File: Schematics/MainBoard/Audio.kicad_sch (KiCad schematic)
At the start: 13 parts, among them J6 AudioJack3, U11 LM386

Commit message: Work on PCB
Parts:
- added C69: 100uF 10V Tant, Capacitor_Tantalum_SMD:CP_EIA-7343-30_AVX-N, symbol Device:C_Polarized
- C46, C55: footprint Capacitor_SMD:C_0603_1608Metric -> Capacitor_SMD:C_0402_1005Metric
- C56: value 250uF 16V -> 100uF 10V Tant; footprint Capacitor_SMD:CP_Elec_10x12.5 -> Capacitor_Tantalum_SMD:CP_EIA-7343-30_AVX-N; LCSC DNF -> DNP; Mouser Part Number 667-EEV-FK1V681Q -> (none)
- LS1: footprint CMS160925078SP67 -> CMS-160925-078SP-67:CMS160925078SP67
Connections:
- net at C45.1, C55.1, C56.1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: now also C69.1
- net at C56.2, LS1.2 (+): now also C69.2
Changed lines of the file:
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@@
+	)
+	(junction
+		(at 229.87 92.71)
+		(diameter 0)
+		(color 0 0 0 0)
 	)
 	(junction
@@
 	)
 	(junction
+		(at 213.36 92.71)
+		(diameter 0)
+		(color 0 0 0 0)
+	)
+	(junction
 		(at 81.28 90.17)
 		(diameter 0)
@@
 	(wire
 		(pts
+			(xy 213.36 92.71) (xy 218.44 92.71)
+		)
+		(stroke
+			(width 0)
+			(type default)
+		)
+	)
+	(wire
+		(pts
 			(xy 156.21 107.95) (xy 163.83 107.95)
 		)
@@
 	(wire
 		(pts
+			(xy 226.06 80.01) (xy 229.87 80.01)
+		)
+		(stroke
+			(width 0)
+			(type default)
+		)
+	)
+	(wire
+		(pts
 			(xy 114.3 166.37) (xy 116.84 166.37)
 		)
@@
 	(wire
 		(pts
+			(xy 213.36 80.01) (xy 213.36 92.71)
+		)
+		(stroke
+			(width 0)
+			(type default)
+		)
+	)
+	(wire
+		(pts
 			(xy 128.27 80.01) (xy 134.62 80.01)
 		)
@@
 	(wire
 		(pts
-			(xy 187.96 92.71) (xy 218.44 92.71)
+			(xy 187.96 92.71) (xy 213.36 92.71)
 		)
 		(stroke
@@
 	(wire
 		(pts
+			(xy 218.44 80.01) (xy 213.36 80.01)
+		)
+		(stroke
+			(width 0)
+			(type default)
+		)
+	)
+	(wire
+		(pts
 			(xy 45.72 140.97) (xy 58.42 140.97)
 		)
@@
 	(wire
 		(pts
+			(xy 229.87 80.01) (xy 229.87 92.71)
+		)
+		(stroke
+			(width 0)
+			(type default)
+		)
+	)
+	(wire
+		(pts
 			(xy 81.28 90.17) (xy 129.54 90.17)
 		)
@@
 	(wire
 		(pts
-			(xy 226.06 92.71) (xy 237.49 92.71)
+			(xy 226.06 92.71) (xy 229.87 92.71)
 		)
 		(stroke
@@
 		(pts
 			(xy 187.96 111.76) (xy 187.96 114.3)
+		)
+		(stroke
+			(width 0)
+			(type default)
+		)
+	)
+	(wire
+		(pts
+			(xy 229.87 92.71) (xy 237.49 92.71)
 		)
 		(stroke
@@
 				(path "/a2243a34-697c-4939-97f7-df548e421864/598e71c9-5c06-425f-ac54-aba71004555d"
 					(reference "#PWR0185")
-					(unit 1)
-				)
-			)
-		)
-	)
-	(symbol
-		(lib_id "Device:C_Polarized")
-		(at 222.25 92.71 90)
-		(unit 1)
-		(exclude_from_sim no)
-		(in_bom yes)
-		(on_board yes)
-		(dnp no)
-		(fields_autoplaced yes)
-		(property "Reference" "C56"
-			(at 221.361 85.09 90)
-			(effects
-				(font
-					(size 1.27 1.27)
-				)
-			)
-		)
-		(property "Value" "250uF 16V"
-			(at 221.361 87.63 90)
-			(effects
-				(font
-					(size 1.27 1.27)
-				)
-			)
-		)
-		(property "Footprint" "Capacitor_SMD:CP_Elec_10x12.5"
-			(at 226.06 91.7448 0)
-			(effects
-				(font
-					(size 1.27 1.27)
-				)
-				(hide yes)
-			)
-		)
-		(property "Datasheet" "~"
-			(at 222.25 92.71 0)
-			(effects
-				(font
-					(size 1.27 1.27)
-				)
-				(hide yes)
-			)
-		)
-		(property "Description" "Polarized capacitor"
-			(at 222.25 92.71 0)
-			(effects
-				(font
-					(size 1.27 1.27)
-				)
-				(hide yes)
-			)
-		)
-		(property "Mouser Part Number" "667-EEV-FK1V681Q"
-			(at 222.25 92.71 90)
-			(effects
-				(font
-					(size 1.27 1.27)
-				)
-				(hide yes)
-			)
-		)
-		(property "LCSC" "DNF"
-			(at 222.25 92.71 90)
-			(effects
-				(font
-					(size 1.27 1.27)
-				)
-				(hide yes)
-			)
-		)
-		(pin "1"
-		)
-		(pin "2"
-		)
-		(instances
-			(project ""
-				(path "/a2243a34-697c-4939-97f7-df548e421864/598e71c9-5c06-425f-ac54-aba71004555d"
-					(reference "C56")
 					(unit 1)
 				)
@@
 	)
 	(symbol
+		(lib_id "Device:C_Polarized")
+		(at 222.25 80.01 90)
+		(unit 1)
+		(exclude_from_sim no)
+		(in_bom yes)
+		(on_board yes)
+		(dnp no)
+		(property "Reference" "C69"
+			(at 220.472 73.66 90)
+			(effects
+				(font
+					(size 1.27 1.27)
+				)
+			)
+		)
+		(property "Value" "100uF 10V Tant"
+			(at 226.314 75.692 90)
+			(effects
+				(font
+					(size 1.27 1.27)
+				)
+			)
+		)
+		(property "Footprint" "Capacitor_Tantalum_SMD:CP_EIA-7343-30_AVX-N"
+			(at 226.06 79.0448 0)
+			(effects
+				(font
+					(size 1.27 1.27)
+				)
+				(hide yes)
+			)
+		)
+		(property "Datasheet" "~"
+			(at 222.25 80.01 0)
+			(effects
+				(font
+					(size 1.27 1.27)
+				)
+				(hide yes)
+			)
+		)
+		(property "Description" "Polarized capacitor"
+			(at 222.25 80.01 0)
+			(effects
+				(font
+					(size 1.27 1.27)
+				)
+				(hide yes)
+			)
+		)
+		(property "LCSC" "DNP"
+			(at 222.25 80.01 0)
+			(effects
+				(font
+					(size 1.27 1.27)
+				)
+				(hide yes)
+			)
+		)
+		(pin "1"
+		)
+		(pin "2"
+		)
+		(instances
+			(project "MainBoard"
+				(path "/a2243a34-697c-4939-97f7-df548e421864/598e71c9-5c06-425f-ac54-aba71004555d"
+					(reference "C69")
+					(unit 1)
+				)
+			)
+		)
+	)
+	(symbol
 		(lib_id "power:GND")
 		(at 121.92 102.87 0)
@@
 			)
 		)
-		(property "Footprint" "CMS160925078SP67"
+		(property "Footprint" "CMS-160925-078SP-67:CMS160925078SP67"
 			(at 248.92 195.25 0)
 			(effects
@@
 			)
 		)
-		(property "Footprint" "Capacitor_SMD:C_0603_1608Metric"
+		(property "Footprint" "Capacitor_SMD:C_0402_1005Metric"
 			(at 128.27 79.0448 0)
 			(effects
@@
 				(path "/a2243a34-697c-4939-97f7-df548e421864/598e71c9-5c06-425f-ac54-aba71004555d"
 					(reference "C46")
+					(unit 1)
+				)
+			)
+		)
+	)
+	(symbol
+		(lib_id "Device:C_Polarized")
+		(at 222.25 92.71 90)
+		(unit 1)
+		(exclude_from_sim no)
+		(in_bom yes)
+		(on_board yes)
+		(dnp no)
+		(property "Reference" "C56"
+			(at 220.472 86.36 90)
+			(effects
+				(font
+					(size 1.27 1.27)
+				)
+			)
+		)
+		(property "Value" "100uF 10V Tant"
+			(at 226.314 88.392 90)
+			(effects
+				(font
+					(size 1.27 1.27)
+				)
+			)
+		)
+		(property "Footprint" "Capacitor_Tantalum_SMD:CP_EIA-7343-30_AVX-N"
+			(at 226.06 91.7448 0)
+			(effects
+				(font
+					(size 1.27 1.27)
+				)
+				(hide yes)
+			)
+		)
+		(property "Datasheet" "~"
+			(at 222.25 92.71 0)
+			(effects
+				(font
+					(size 1.27 1.27)
+				)
+				(hide yes)
+			)
+		)
+		(property "Description" "Polarized capacitor"
+			(at 222.25 92.71 0)
+			(effects
+				(font
+					(size 1.27 1.27)
+				)
+				(hide yes)
+			)
+		)
+		(property "LCSC" "DNP"
+			(at 222.25 92.71 0)
+			(effects
+				(font
+					(size 1.27 1.27)
+				)
+				(hide yes)
+			)
+		)
+		(pin "1"
+		)
+		(pin "2"
+		)
+		(instances
+			(project "MainBoard"
+				(path "/a2243a34-697c-4939-97f7-df548e421864/598e71c9-5c06-425f-ac54-aba71004555d"
+					(reference "C56")
 					(unit 1)
 				)
@@
 			)
 		)
-		(property "Footprint" "Capacitor_SMD:C_0603_1608Metric"
+		(property "Footprint" "Capacitor_SMD:C_0402_1005Metric"
 			(at 188.9252 101.6 0)
 			(effects

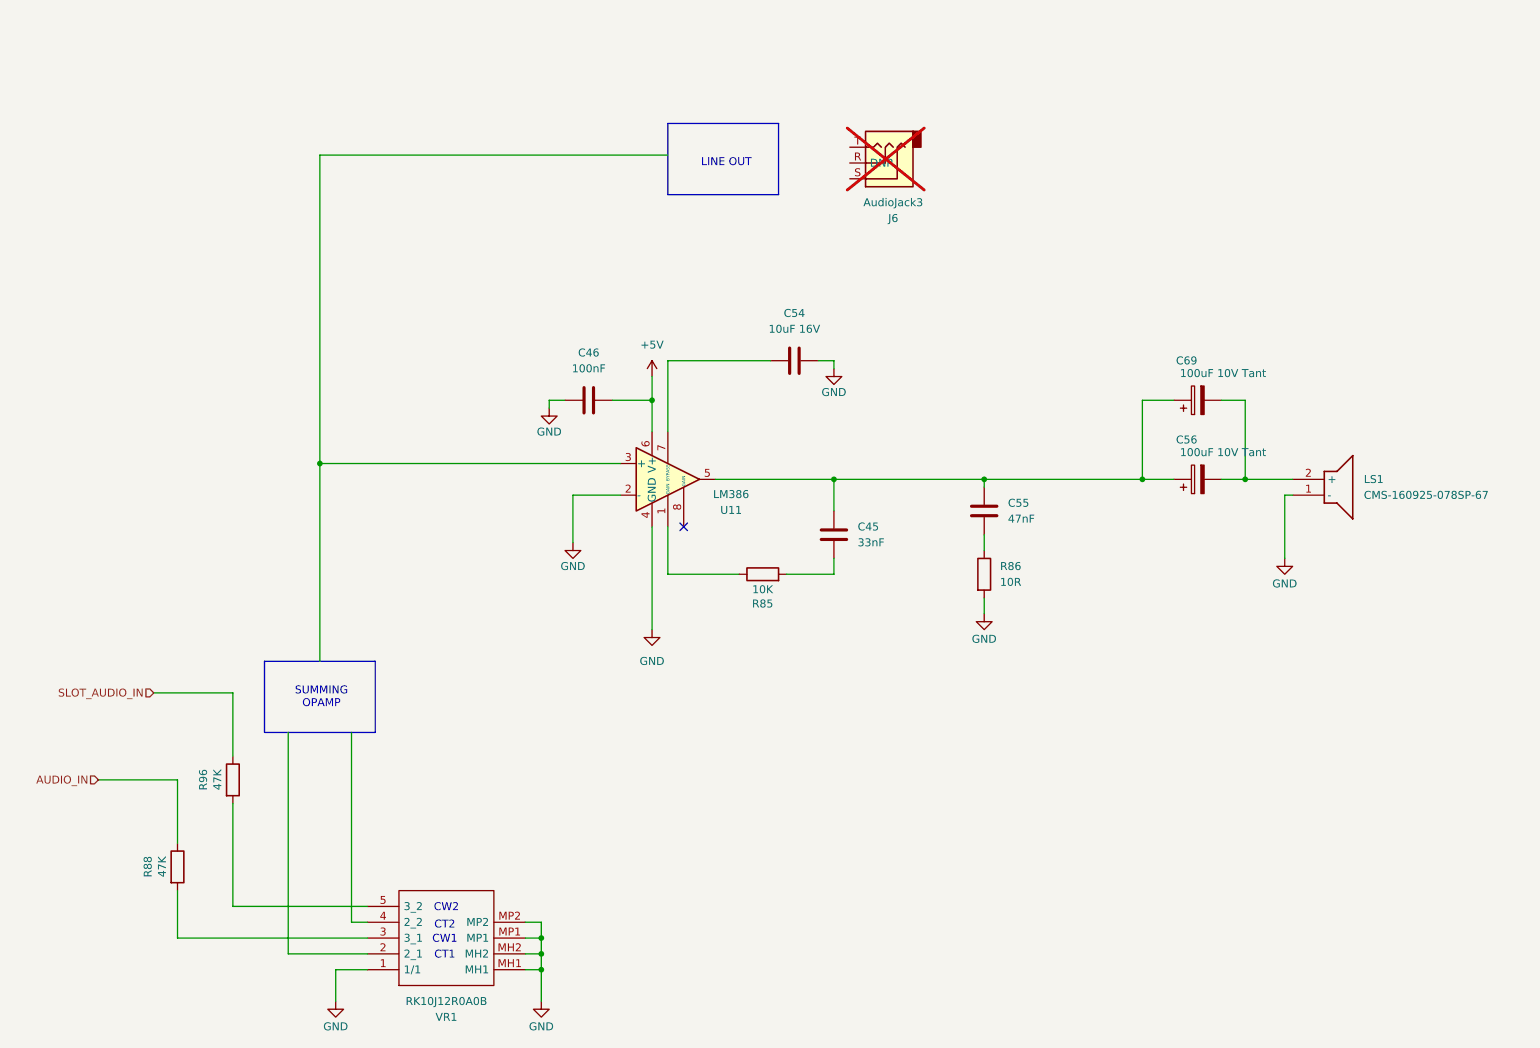
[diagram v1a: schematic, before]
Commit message: Work on PCB routing, added SwinSID
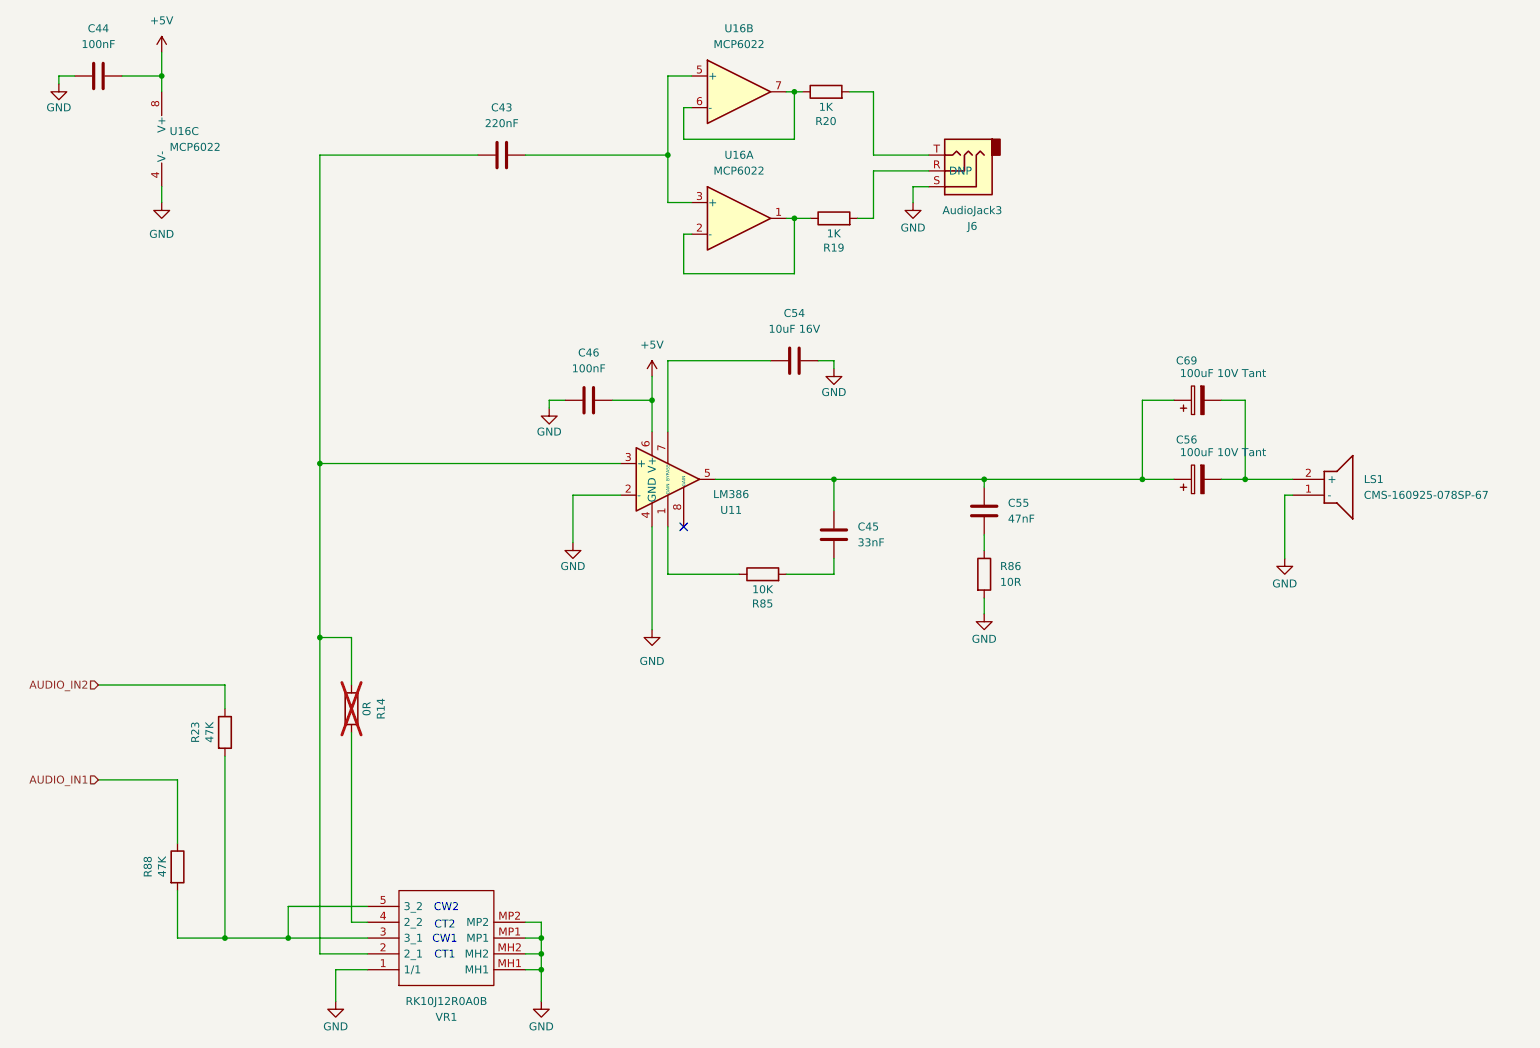
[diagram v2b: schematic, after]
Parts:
- removed R96: 47K, Resistor_SMD:R_0402_1005Metric, symbol Device:R
- added C43: 220nF, Capacitor_SMD:C_0603_1608Metric, symbol Device:C
- added C44: 100nF, Capacitor_SMD:C_0402_1005Metric, symbol Device:C
- added R14: 0R, Resistor_SMD:R_0402_1005Metric, symbol Device:R
- added R19, R20: 1K, Resistor_SMD:R_0402_1005Metric, symbol Device:R
- added R23: 47K, Resistor_SMD:R_0402_1005Metric, symbol Device:R
- added U16: MCP6022, Package_SO:SOIC-8_3.9x4.9mm_P1.27mm, symbol Amplifier_Operational:MCP6022
- J6: now fitted
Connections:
- net +5V: now also C44.2, U16.8 (V+)
- net GND: now also J6.S, C44.1, U16.4 (V-)
- net at J6.R: now also R19.2
- net at J6.T: now also R20.2
- net at VR1.2 (2_1): now also U11.3 (+), C43.1, R14.2
- net at R88.2, VR1.3 (3_1): now also VR1.5 (3_2), R23.2
- net at VR1.4 (2_2): now also R14.1
- net AUDIO_IN renamed AUDIO_IN1
- new net: R19.1, U16.1, U16.2 (-)
- new net: C43.2, U16.3 (+), U16.5 (+)
- new net: R20.1, U16.6 (-), U16.7
- new net AUDIO_IN2: R23.1
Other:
- note removed: "LINE OUT"
- note removed: "SUMMING OPAMP"

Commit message: Updates based on production files for JLC
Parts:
- C43: LCSC (none) -> C21120
- C44, C46: LCSC C113803 -> C307331
- C55: LCSC C1622 -> C82219
- C56, C69: LCSC DNP -> C49332976
- J6: LCSC DNP -> DNF; now not fitted
- LS1: now not fitted
- R19, R20: LCSC (none) -> C11702
- R23, R88: LCSC DNF -> C25792
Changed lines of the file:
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@@
 		(in_bom yes)
 		(on_board yes)
-		(dnp no)
+		(dnp yes)
 		(property "Reference" "J6"
 			(at 186.055 52.07 0)
@@
 			)
 		)
-		(property "LCSC" "DNP"
+		(property "LCSC" "DNF"
 			(at 184.15 43.18 0)
 			(effects
@@
 			)
 		)
-		(property "LCSC" "DNF"
+		(property "LCSC" "C25792"
 			(at 58.42 154.94 90)
 			(effects
@@
 			)
 		)
-		(property "LCSC" ""
+		(property "LCSC" "C11702"
 			(at 163.83 50.8 90)
 			(effects
@@
 			)
 		)
-		(property "LCSC" "DNP"
+		(property "LCSC" "C49332976"
 			(at 222.25 80.01 0)
 			(effects
@@
 			)
 		)
-		(property "LCSC" ""
+		(property "LCSC" "C21120"
 			(at 110.49 40.64 0)
 			(effects
@@
 			)
 		)
-		(property "LCSC" "C113803"
+		(property "LCSC" "C307331"
 			(at 45.72 27.94 0)
 			(effects
@@
 			)
 		)
-		(property "LCSC" ""
+		(property "LCSC" "C11702"
 			(at 162.56 30.48 90)
 			(effects
@@
 		(in_bom yes)
 		(on_board yes)
-		(dnp no)
+		(dnp yes)
 		(fields_autoplaced yes)
 		(property "Reference" "LS1"
@@
 			)
 		)
-		(property "LCSC" "DNF"
+		(property "LCSC" "C25792"
 			(at 66.04 133.35 90)
 			(effects
@@
 			)
 		)
-		(property "LCSC" "C113803"
+		(property "LCSC" "C307331"
 			(at 124.46 80.01 0)
 			(effects
@@
 			)
 		)
-		(property "LCSC" "DNP"
+		(property "LCSC" "C49332976"
 			(at 222.25 92.71 0)
 			(effects
@@
 			)
 		)
-		(property "LCSC" "C1622"
+		(property "LCSC" "C82219"
 			(at 187.96 97.79 0)
 			(effects
